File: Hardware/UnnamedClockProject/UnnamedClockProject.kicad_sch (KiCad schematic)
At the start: 34 parts, among them J101 CLOCK_OUT, J102 POWER, J103 BUTTONS, Q101 2N3904, U104 G3MB-202P, U105 G3MB-202P, U106 G3MB-202P, U107 CAT24C256

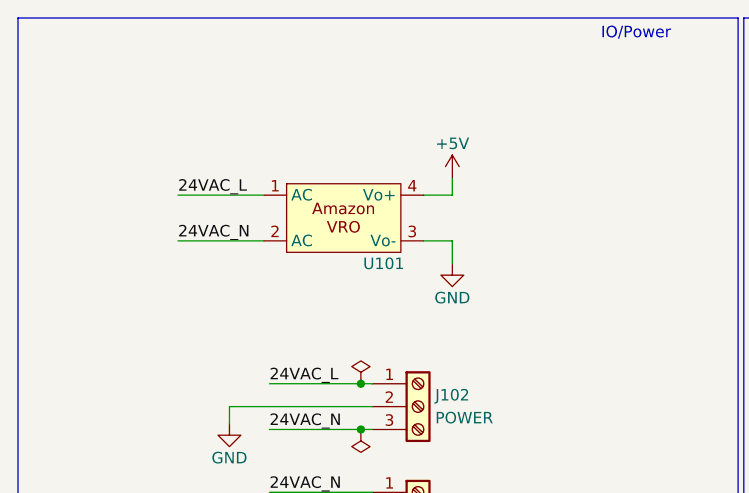
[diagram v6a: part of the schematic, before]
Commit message: Add amazon dro from upstream, fix logos and prep for RC2
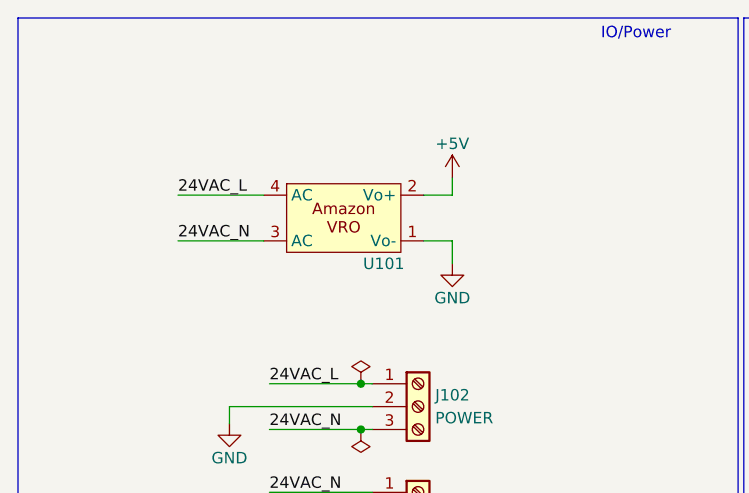
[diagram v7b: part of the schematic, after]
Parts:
- U101: footprint (none) -> ac1ja:Amazon_DRO
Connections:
- net +5V: now also U101.2 (Vo+); no longer U101.4 (Vo+)
- net 24VAC_L: now also U101.4 (AC); no longer U101.1 (AC)
- net 24VAC_N: now also U101.3 (AC); no longer U101.2 (AC)
- net GND: now also U101.1 (Vo-); no longer U101.3 (Vo-)
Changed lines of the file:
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@@
       (effects (font (size 1.27 1.27)))
     )
-    (property "Footprint" "" (at 49.53 34.925 0)
+    (property "Footprint" "ac1ja:Amazon_DRO" (at 49.53 34.925 0)
       (effects (font (size 1.27 1.27)) hide)
     )

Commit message: Add 3d models
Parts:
- J101, J102: footprint TerminalBlock_WAGO:TerminalBlock_WAGO_236-103_1x03_P5.00mm_45Degree -> TerminalBlock_Phoenix:TerminalBlock_Phoenix_MKDS-1,5-3_1x03_P5.00mm_Horizontal
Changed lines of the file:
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@@
       (effects (font (size 1.27 1.27)) (justify left))
     )
-    (property "Footprint" "TerminalBlock_WAGO:TerminalBlock_WAGO_236-103_1x03_P5.00mm_45Degree" (at 57.785 55.88 0)
+    (property "Footprint" "TerminalBlock_Phoenix:TerminalBlock_Phoenix_MKDS-1,5-3_1x03_P5.00mm_Horizontal" (at 57.785 55.88 0)
       (effects (font (size 1.27 1.27)) hide)
     )
@@
       (effects (font (size 1.27 1.27)) (justify left))
     )
-    (property "Footprint" "TerminalBlock_WAGO:TerminalBlock_WAGO_236-103_1x03_P5.00mm_45Degree" (at 57.785 67.945 0)
+    (property "Footprint" "TerminalBlock_Phoenix:TerminalBlock_Phoenix_MKDS-1,5-3_1x03_P5.00mm_Horizontal" (at 57.785 67.945 0)
       (effects (font (size 1.27 1.27)) hide)
     )
